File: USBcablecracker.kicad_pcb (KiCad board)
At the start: 2 copper layers, 100 x 71 mm, 52 parts, among them IC1 ATTINY85-S, P1 USB_A_L, P10 USB_A_R, P11 USB_B_R, P12 CONN_01X06, P2 USB_B_L, P3 USB_TYPEC-S, P4 USB_MINI_L, P5 USB_MICRO_L, P6 USB_OTG, P7 USB_MINI_R, P8 USB_MICRO_R, P9 USB_TYPEC-S, Q1 S8050, SW1 Switch_SPDT_x2, U1 PCF8574, U2 LMV358, U3 AD623

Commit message: update pcb
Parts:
- removed D5: BLUE, LEDs:LED_0603
- removed D6: RED, LEDs:LED_0603
- removed IC1: ATTINY85-S, Housings_SOIC:SOIJ-8_5.3x5.3mm_Pitch1.27mm
- removed Q1: S8050, TO_SOT_Packages_SMD:SOT-23_Handsoldering
- removed R20: 470R, Resistors_SMD:R_0603_HandSoldering
- removed R21: 1K, Resistors_SMD:R_0603_HandSoldering
- removed RV1: POT, USBcablecracker:BOURNS-3362P_pot
- added C7: 1uF, Capacitors_SMD:C_0603_HandSoldering, B.Cu at (74.5, 74.4)
- added C8: 22uF, Capacitors_Tantalum_SMD:Tantalum_Case-A_EIA-3216-18_Wave, B.Cu at (74.6, 81.8)
- added C9: 100nF, Capacitors_SMD:C_0603_HandSoldering, B.Cu at (74.4, 78.9)
- added CONN1: ICSP, Connectors:CONN_2.54mm_2x3, F.Cu at (59.1, 62.5)
- added CONN2: USB_B, SmartEye:USB_Micro-B, F.Cu at (52.6, 85.4)
- added D4: ON, LEDs:LED_0603, F.Cu at (53.4, 76.9)
- added R10: 91R, Resistors_SMD:R_0603_HandSoldering, B.Cu at (113.0, 75.7)
- added Y1: 16MHz, Crystals:crystal_FA238-TSX3225, B.Cu at (75.6, 85.8)
- C1: value 0.1uF -> 22P
- C5: value 4.7uF -> 22P; moved to B.Cu
- C6: value 0.1uF -> 100nF; moved to B.Cu
- D1: value S4 -> RX; footprint AirBox:SOD-323 -> LEDs:LED_0603; moved to F.Cu
- D2: value W4 -> TX; footprint AirBox:SOD-323 -> LEDs:LED_0603; moved to F.Cu
- D3: value W4 -> L; footprint AirBox:SOD-323 -> LEDs:LED_0603; moved to F.Cu
- P12: value CONN_01X06 -> CONN_01X09; footprint Pin_Headers:Pin_Header_Straight_1x06 -> Connectors:CONN_2.54mm_1x9
- P6: value USB_OTG -> CONN_01X09; footprint SmartEye:USB_Micro-B -> Connectors:CONN_2.54mm_1x9
- R13: value 10K -> 100K
- R17: value 10K -> 100R
- R2, R3, R5: value 10K -> 1K; moved to F.Cu
- R4: moved to F.Cu
- R6: value 10K -> 1K
- R7: value 1.5K -> 22R; moved to F.Cu
- R8: value 68R -> 22R; moved to F.Cu
- R9: value 68R -> 10K
- U1: value PCF8574 -> ATmega32U4-AU; footprint Housings_SOIC:SOIC-16W_7.5x10.3mm_Pitch1.27mm -> Housings_QFP:TQFP-44_10x10mm_Pitch0.8mm
- moved P6 85.6 mm to (135.5, 64.7), turned to 0 degrees
- moved P12 83.1 mm to (135.3, 106.5)
- moved R1 56.5 mm to (135.0, 73.2), turned to 90 degrees
- moved R5 46.8 mm to (58.8, 76.9), turned to 0 degrees
- moved R4 46.7 mm to (58.8, 74.7), turned to 0 degrees
- moved G*** 39.9 mm to (113.8, 107.7), turned to 180 degrees
- moved C6 38.4 mm to (98.9, 85.7), turned to 90 degrees
- moved C1 34.9 mm to (71.7, 86.0), turned to 270 degrees
- moved D3 26.2 mm to (53.4, 74.7), turned to 0 degrees
- moved D2 25.6 mm to (53.4, 72.5)
- moved D1 24.9 mm to (53.4, 70.4), turned to 180 degrees
- moved R2 23.3 mm to (58.8, 70.4), turned to 0 degrees
- moved R3 21.4 mm to (58.8, 72.5), turned to 0 degrees
- moved R8 20.0 mm to (61.1, 84.2)
- moved R9 19.1 mm to (74.5, 76.6), turned to 0 degrees
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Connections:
- C1 pad 1: +5V -> Net-(C1-Pad1)
- C5 pad 1: +5V -> Net-(C5-Pad1)
- C6 pad 1: +5V -> /AREF
- D1 pad 2: +5V -> +5C
- D2 pad 2: GND -> +5C
- D3 pad 1: Net-(D3-Pad1) -> GND
- D3 pad 2: GND -> Net-(D3-Pad2)
- DS1 pad 11: /DB4 -> /D6
- DS1 pad 12: /DB5 -> /D7
- DS1 pad 13: /DB6 -> /IO11
- DS1 pad 14: /DB7 -> /IO12
- DS1 pad 15: /A -> +5C
- DS1 pad 16: /K -> Net-(DS1-Pad16)
- DS1 pad 2: +5V -> +5C
- DS1 pad 3: /VO -> Net-(DS1-Pad16)
- DS1 pad 4: /RS -> /D4
- DS1 pad 5: /RW -> GND
- DS1 pad 6: /CS -> /D5
- P12 pad 1: /AREF -> +5C
- P12 pad 2: Net-(D5-Pad2) -> GND
- P12 pad 3: /SDA -> /IO13
- P12 pad 4: /SCL -> /IO10
- P12 pad 5: Net-(IC1-Pad3) -> /IO9
- P12 pad 6: Net-(IC1-Pad1) -> /D3
- P6 pad 1: Net-(D1-Pad1) -> +5C
- P6 pad 2: Net-(D3-Pad1) -> GND
- P6 pad 3: Net-(D2-Pad1) -> /RESET
- P6 pad 4: Net-(P6-Pad4) -> /A5
- P6 pad 5: GND -> /A4
- P6 pad 6: GND -> /A3
- R1 pad 1: Net-(R1-Pad1) -> +5C
- R1 pad 2: +5V -> /RESET
- R2 pad 1: Net-(R2-Pad1) -> Net-(D1-Pad1)
- R2 pad 2: +5V -> /RX_LED
- R3 pad 1: Net-(R3-Pad1) -> Net-(D2-Pad1)
- R3 pad 2: +5V -> /TX_LED
- R4 pad 1: +5V -> Net-(D3-Pad2)
- R4 pad 2: /P3 -> /IO13
- R5 pad 1: +5V -> Net-(D4-Pad2)
- R5 pad 2: /SCL -> +5C
- R6 pad 1: +5V -> GND
- R6 pad 2: /SDA -> /HWB
- R7 pad 1: +5V -> /D+
- R7 pad 2: Net-(D3-Pad1) -> Net-(CONN2-Pad3)
- R8 pad 1: /SCL -> /D-
- R8 pad 2: Net-(D3-Pad1) -> Net-(CONN2-Pad2)
- R9 pad 1: Net-(IC1-Pad3) -> GND
- R9 pad 2: Net-(D2-Pad1) -> +5C
- U1 pad 1: Net-(R1-Pad1) -> /D7
- U1 pad 10: /DB5 -> /MOSI
- U1 pad 11: /DB6 -> /MISO
- U1 pad 12: /DB7 -> /IO11
- U1 pad 13: Net-(U1-Pad13) -> /RESET
- U1 pad 14: /SCL -> +5C
- U1 pad 15: /SDA -> GND
- U1 pad 16: +5V -> Net-(C5-Pad1)
- U1 pad 2: Net-(R2-Pad1) -> +5C
- U1 pad 3: Net-(R3-Pad1) -> /D-
- U1 pad 4: /RS -> /D+
- U1 pad 5: /RW -> GND
- U1 pad 6: /CS -> +5C
- U1 pad 7: /P3 -> +5C
- U1 pad 8: GND -> /RX_LED
- U1 pad 9: /DB4 -> /SCK
- U2 pad 8: +5V -> +5C
- U3 pad 6: /TO_ADC -> /IO8
- U3 pad 7: +5V -> +5C
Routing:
- net +5C: track 0.00 -> 264.8 mm, vias 0 -> 1
- net +5V: track 178.3 -> 0.00 mm
- net /RESET: track 0.00 -> 133.2 mm, vias 0 -> 2
- net /IO13: track 0.00 -> 105.8 mm, vias 0 -> 1
- net /SDA: track 96.2 -> 0.00 mm, vias 2 -> 0
- net /SCL: track 93.9 -> 0.00 mm, vias 2 -> 0
- net /D1: track 0.00 -> 67.2 mm
- net /D3: track 0.00 -> 66.5 mm
- net /D2: track 0.00 -> 65.6 mm
- net Net-(D5-Pad2): track 64.1 -> 0.00 mm, vias 1 -> 0
- net /D0: track 0.00 -> 62.1 mm
- net /IO10: track 0.00 -> 61.7 mm, vias 0 -> 1
- net /IO9: track 0.00 -> 60.3 mm, vias 0 -> 1
- net /A5: track 0.00 -> 59.7 mm, vias 0 -> 1
- net /AREF: track 101.3 -> 44.7 mm, vias 2 -> 3
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- removed copper zone on B.Cu, net GND
- removed copper zone on F.Cu, net GND
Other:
- net class power added: clearance 0.2, trace_width 0.4, via_dia 0.6, via_drill 0.4
- board text added: "13"
- board text added: "P"
- board text added: "R"
- board text added: "T"
- board text added: "v0.2"
- board text removed: "SCL"
- board text removed: "SDA"
- board text removed: "v0.1"

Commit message: update pcb
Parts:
- moved G*** 3.38 mm to (114.9, 104.5)
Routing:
- net GND: track 318.9 -> 472.8 mm, vias 1 -> 23
- net /D7: track 31.2 -> 36.4 mm
- net /D0: track 62.1 -> 65.8 mm
- net /IO11: track 34.8 -> 38.0 mm
- net /A5: track 59.7 -> 61.3 mm
- net /TP2: track 136.8 -> 138.2 mm
- net /D2: track 65.6 -> 66.7 mm
- net /D5: track 11.5 -> 10.8 mm
- net /D4: track 11.6 -> 10.9 mm
- net /MOSI: track 44.7 -> 45.3 mm
- net Net-(DS1-Pad16): track 40.1 -> 39.5 mm
- added copper zone on B.Cu, net GND
- added copper zone on F.Cu, net GND
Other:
- net class Default: trace_width 0.4 -> 0.3

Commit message: check
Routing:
- net GND: track 472.8 -> 586.8 mm, vias 23 -> 33
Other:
- board text added: "A0"
- board text added: "A1"
- board text added: "A2"
- board text added: "A3"
- board text added: "A4"
- board text added: "A5"
- board text added: "D0"
- board text added: "D1"
- board text added: "D10"
- board text added: "D13"
- board text added: "D2"
- board text added: "D3"
- board text added: "D9"
- board text added: "G"
- board text added: "RES"
- board text added: "USBcablecracker"
- board text added: "VCC"

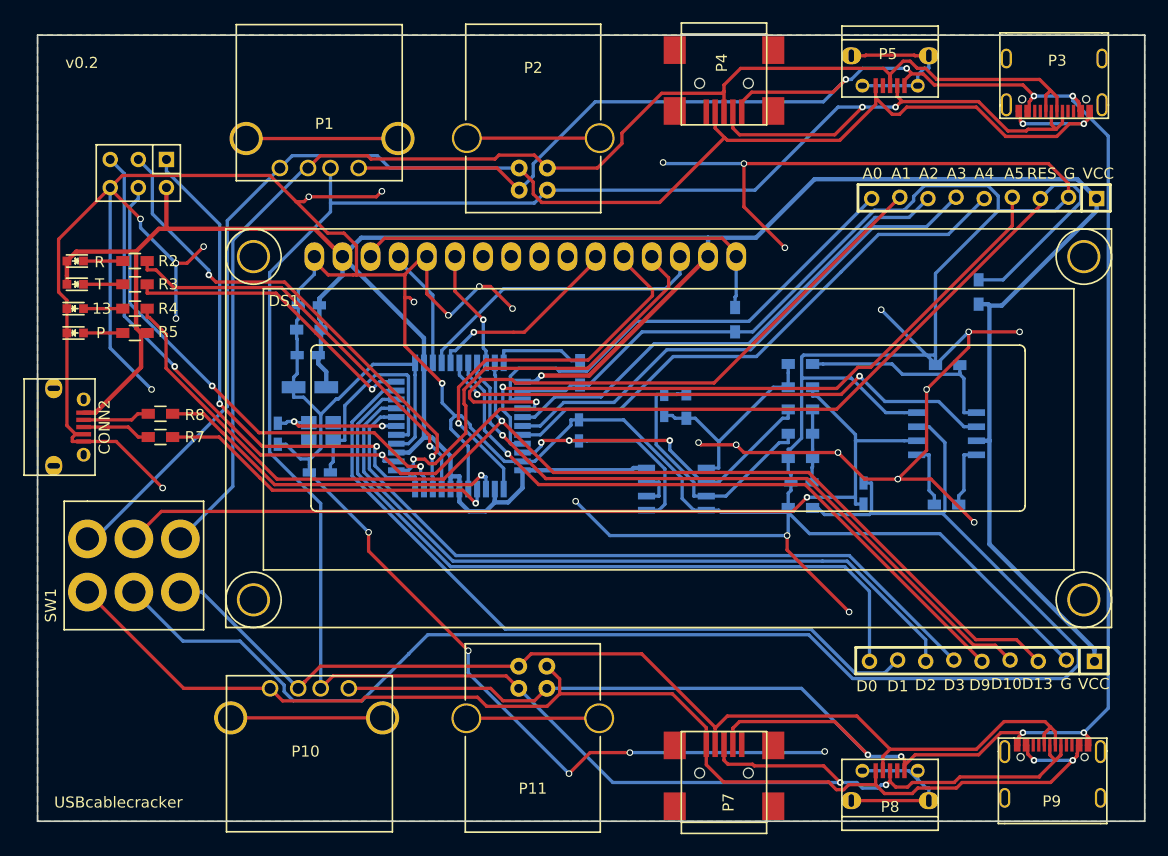
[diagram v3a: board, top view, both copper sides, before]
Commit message: Version 0.4 finished. Solved UCAP inner linear regulator problem. Modified library, footprints, instrumentation amplifier common mode input voltage, modified AREF output load.
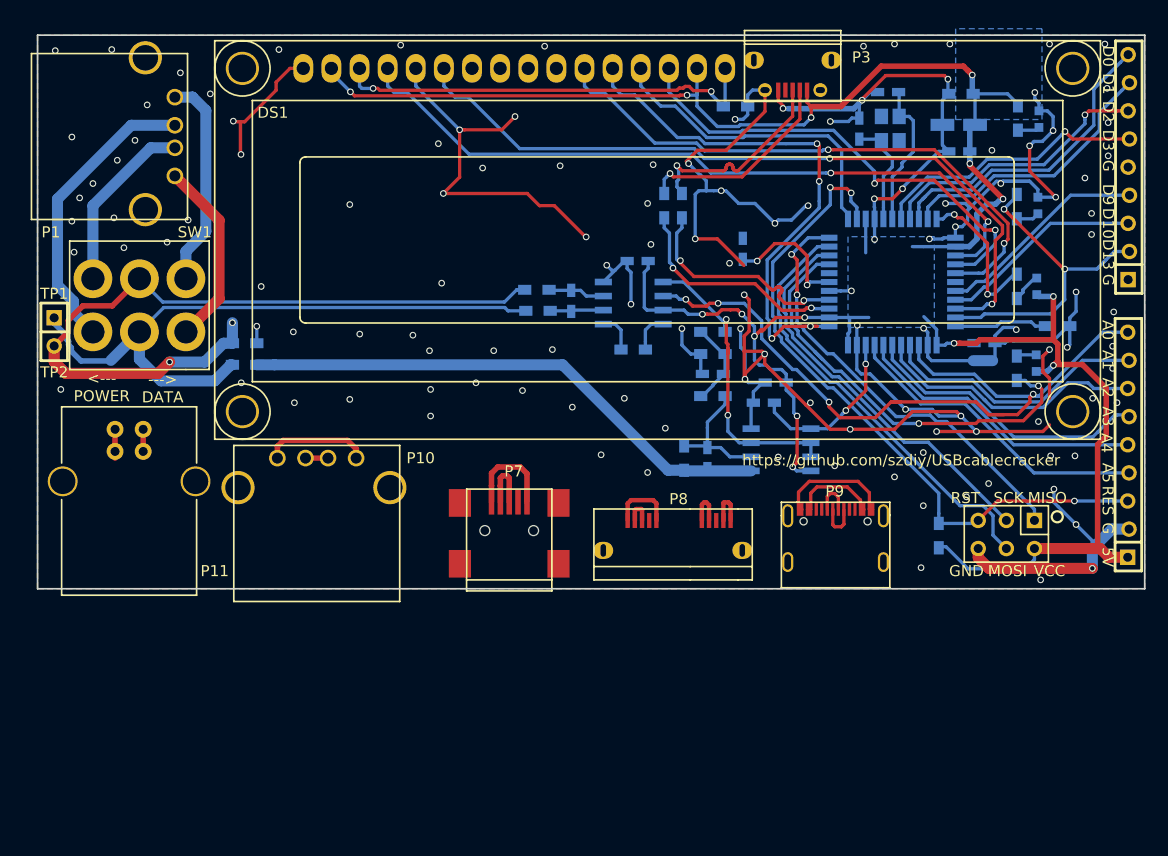
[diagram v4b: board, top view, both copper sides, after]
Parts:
- removed the P3 at (141.5, 53.5)
- removed P4: USB_MINI_L, Connect:USB_Mini-B
- removed P5: USB_MICRO_L, SmartEye:USB_Micro-B
- added C10: 100nF, Capacitors_SMD:C_0603_HandSoldering, B.Cu at (116.7, 81.4)
- added C11: 100nF, Capacitors_SMD:C_0603_HandSoldering, B.Cu at (104.2, 70.4)
- added C12: 100nF, Capacitors_SMD:C_0603_HandSoldering, B.Cu at (135.5, 77.8)
- C1, C5: value 22P -> 15P
- D1, D2, D3, D4, R2, R3, R4, R5, R7, R8: moved to B.Cu
- P1: value USB_A_L -> USB_A; footprint Connect:USB_A -> USBcablecracker:USB_A
- P10: value USB_A_R -> USB_A; footprint Connect:USB_A -> USBcablecracker:USB_A
- P11: value USB_B_R -> USB_B; footprint Connect:USB_B -> USBcablecracker:USB_B
- P12, P6: footprint Connectors:CONN_2.54mm_1x9 -> USBcablecracker:CONN_2.54mm_1x9
- P2: value USB_B_L -> CONN_01X02; footprint Connect:USB_B -> Connectors:CONN_2.54mm_1x2
- P3: renamed from CONN2; value USB_B -> USB_B-Micro; footprint SmartEye:USB_Micro-B -> USBcablecracker:USB_Micro-B
- P7: value USB_MINI_R -> USB_B-Mini; footprint Connect:USB_Mini-B -> USBcablecracker:USB_Mini-B
- P8: value USB_MICRO_R -> USB_B-Micro-3.0; footprint SmartEye:USB_Micro-B -> USBcablecracker:USB_Micro-30
- R15, R16: value 1K -> 10K
- R17: value 100R -> 220
- R18: value 100R -> 150
- R19: value 100R -> 10k
- moved D4 89.2 mm to (140.4, 57.6), turned to 270 degrees
- moved D3 87.4 mm to (140.3, 65.4), turned to 270 degrees
- moved D1 87.3 mm to (140.2, 79.6), turned to 270 degrees
- moved D2 86.8 mm to (140.2, 72.7), turned to 270 degrees
- moved CONN1 84.9 mm to (137.5, 95.1)
- moved R5 82.1 mm to (138.5, 57.5), turned to 90 degrees
- moved R2 80.2 mm to (138.4, 80.1), turned to 270 degrees
- moved R4 80.2 mm to (138.4, 65.5), turned to 90 degrees
- moved R3 79.6 mm to (138.4, 72.7), turned to 90 degrees
- moved P3 73.0 mm to (118.2, 53.4), turned to 180 degrees
- moved C8 63.2 mm to (133.2, 58.1)
- moved C1 63.2 mm to (126.8, 55.1), turned to 180 degrees
- moved R9 62.6 mm to (133.4, 55.3)
- moved C9 61.7 mm to (133.2, 60.5)
- moved Y1 58.2 mm to (127.0, 58.4), turned to 270 degrees
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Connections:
- net Net-(C1-Pad1) renamed /X+
- net Net-(C5-Pad1) renamed /X-
- net Net-(CONN2-Pad2) renamed /DIN-
- net Net-(CONN2-Pad3) renamed /DIN+
- C4 pad 1: /TP1 -> Net-(C4-Pad1)
- C4 pad 2: /TP2 -> Net-(C4-Pad2)
- C7 pad 2: +5C -> Net-(C7-Pad2)
- C8 pad 1: +5C -> +5V
- C9 pad 2: +5C -> +5V
- CONN1 pad 2: +5C -> +5V
- D1 pad 2: +5C -> +5V
- D2 pad 2: +5C -> +5V
- DS1 pad 15: +5C -> +5V
- DS1 pad 2: +5C -> +5V
- P1 pad 1: /TEST1 -> Net-(P1-Pad1)
- P1 pad 2: /TEST2 -> Net-(P1-Pad2)
- P1 pad 3: /TEST3 -> Net-(P1-Pad3)
- P1 pad 4: /TEST4 -> Net-(P1-Pad4)
- P10 pad 1: /TEST5 -> Net-(P10-Pad1)
- P10 pad 2: /TEST6 -> Net-(P10-Pad2)
- P10 pad 3: /TEST2 -> Net-(P10-Pad2)
- P10 pad 4: /TEST1 -> Net-(P10-Pad1)
- P11 pad 1: /TEST5 -> Net-(P11-Pad1)
- P11 pad 2: /TEST6 -> Net-(P11-Pad2)
- P11 pad 3: /TEST2 -> Net-(P11-Pad2)
- P11 pad 4: /TEST1 -> Net-(P11-Pad1)
- P12 pad 1: +5C -> GND
- P12 pad 2: GND -> /IO13
- P12 pad 3: /IO13 -> /IO10
- P12 pad 4: /IO10 -> /IO9
- P12 pad 5: /IO9 -> GND
- P2 pad 1: /TEST1 -> /TP1
- P2 pad 2: /TEST2 -> /TP2
- P3 pad 1: +5C -> +5V
- P3 pad 4: GND -> Net-(P3-Pad4)
- P3 pad 6: (no net) -> GND
- P6 pad 1: +5C -> +5V
- P7 pad 1: /TEST5 -> Net-(P7-Pad1)
- P7 pad 2: /TEST6 -> Net-(P7-Pad2)
- P7 pad 3: /TEST2 -> Net-(P7-Pad2)
- P7 pad 4: /TEST1 -> Net-(P7-Pad4)
- P7 pad 5: Net-(P7-Pad5) -> Net-(P7-Pad1)
- P7 pad 6: (no net) -> Net-(P7-Pad6)
- P8 pad 1: /TEST5 -> Net-(P8-Pad1)
- P8 pad 2: /TEST6 -> Net-(P8-Pad2)
- P8 pad 3: /TEST2 -> Net-(P8-Pad2)
- P8 pad 5: /TEST1 -> Net-(P8-Pad1)
- P9 pad 1: (no net) -> Net-(P9-Pad1)
- P9 pad 2: (no net) -> Net-(P9-Pad2)
- P9 pad 3: (no net) -> Net-(P9-Pad3)
- P9 pad 4: (no net) -> Net-(P9-Pad4)
- R1 pad 1: +5C -> +5V
- R11 pad 1: /AREF -> /REFO
- R15 pad 1: Net-(C3-Pad1) -> Net-(C4-Pad1)
- R15 pad 2: /VOL_HALF -> /TP1
- R16 pad 1: /VOL_HALF -> Net-(C4-Pad2)
- R16 pad 2: GND -> /TP2
- R5 pad 2: +5C -> +5V
- R9 pad 2: +5C -> +5V
- SW1 pad 1: /TEST4 -> Net-(P1-Pad4)
- SW1 pad 3: /TEST3 -> Net-(P1-Pad2)
- SW1 pad 4: /TEST5 -> Net-(P1-Pad1)
- SW1 pad 6: /TEST6 -> Net-(P1-Pad3)
- U1 pad 14: +5C -> +5V
- U1 pad 2: +5C -> +5V
- U1 pad 24: +5C -> +5V
- U1 pad 34: +5C -> +5V
- U1 pad 44: +5C -> +5V
- U1 pad 6: +5C -> Net-(C7-Pad2)
- U2 pad 2: /AREF -> Net-(C3-Pad2)
- U2 pad 3: Net-(C3-Pad2) -> /REFO
- U2 pad 6: Net-(U2-Pad6) -> /REFO
- U2 pad 7: Net-(U2-Pad6) -> /REFO
- U2 pad 8: +5C -> +5V
- U3 pad 2: /TP1 -> Net-(C4-Pad1)
- U3 pad 3: /TP2 -> Net-(C4-Pad2)
- U3 pad 5: /VOL_HALF -> /REFO
- U3 pad 6: /IO8 -> /A0
- U3 pad 7: +5C -> +5V
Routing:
- net GND: track 586.8 -> 308.4 mm, vias 33 -> 50
- net +5C: track 264.7 -> 0.00 mm, vias 1 -> 0
- net /TEST2: track 232.2 -> 4.17 mm, vias 4 -> 0
- net /TEST1: track 238.7 -> 10.9 mm, vias 8 -> 0
- net +5V: track 0.00 -> 213.0 mm, vias 0 -> 15
- net /TEST4: track 136.9 -> 0.00 mm, vias 2 -> 0
- net /TEST3: track 120.7 -> 0.00 mm
- net /TEST5: track 113.6 -> 8.15 mm, vias 2 -> 0
- net /TEST6: track 98.3 -> 3.53 mm
- net /IO13: track 105.8 -> 29.5 mm, vias 1 -> 2
- net /RESET: track 133.2 -> 61.6 mm, vias 2 -> 3
- net /TP2: track 138.2 -> 68.1 mm, vias 0 -> 2
- net /D5: track 10.8 -> 68.2 mm, vias 1 -> 2
- net /D4: track 10.9 -> 66.3 mm, vias 0 -> 2
- net /IO8: track 51.2 -> 0.00 mm, vias 2 -> 0
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- added copper zone on B.Cu, net +5V
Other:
- board size 100 x 71 mm -> 100 x 50 mm
- rule trace_min: 0.2 -> 0.3
- board text added: "---> DATA"
- board text added: "5V"
- board text added: "<--- POWER"
- board text added: "GND"
- board text added: "MISO"
- board text added: "MOSI"
- board text added: "PWR"
- board text added: "RST"
- board text added: "RX"
- board text added: "SCK"
- board text added: "SZDIY COMMUNITY 2009.4.19-2017.4.19"
- board text added: "TP1"
- board text added: "TP2"
- board text added: "TX"
- board text added: "https://github.com/szdiy/USBcablecracker"
- board text removed: "13"
- board text removed: "P"
- board text removed: "R"
- board text removed: "T"
- board text removed: "USBcablecracker"
- board text removed: "v0.2"

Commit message: fangzhou
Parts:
- moved G*** 0.22 mm to (78.9, 66.6)
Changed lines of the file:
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@@
     (links 149)
     (no_connects 0)
-    (area 49.924999 49.924999 150.075001 100.075001)
+    (area 47.6808 47.625 152.53256 101.955)
     (thickness 1.6)
     (drawings 39)
@@
   )
   (module USBcablecracker:donotcare (layer B.Cu)
-    (at 78.8 66.8 180)
+    (at 78.9 66.6 180)
     (fp_text reference G*** (at 0 0 180) (layer B.SilkS) hide
       (effects (font (thickness 0.3)) (justify mirror))

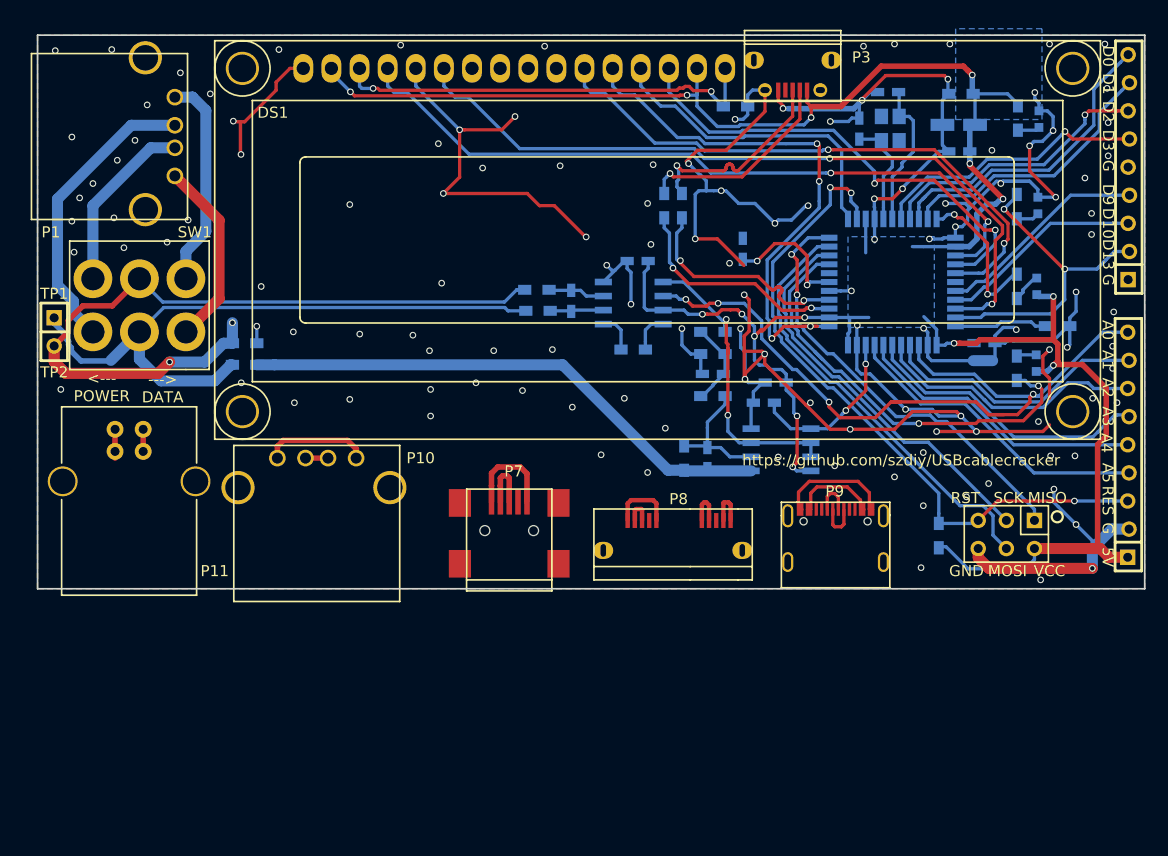
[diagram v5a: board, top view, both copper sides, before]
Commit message: Modified two 9-pin header distance and modified all via with not net to net GND. Add gitinore file.
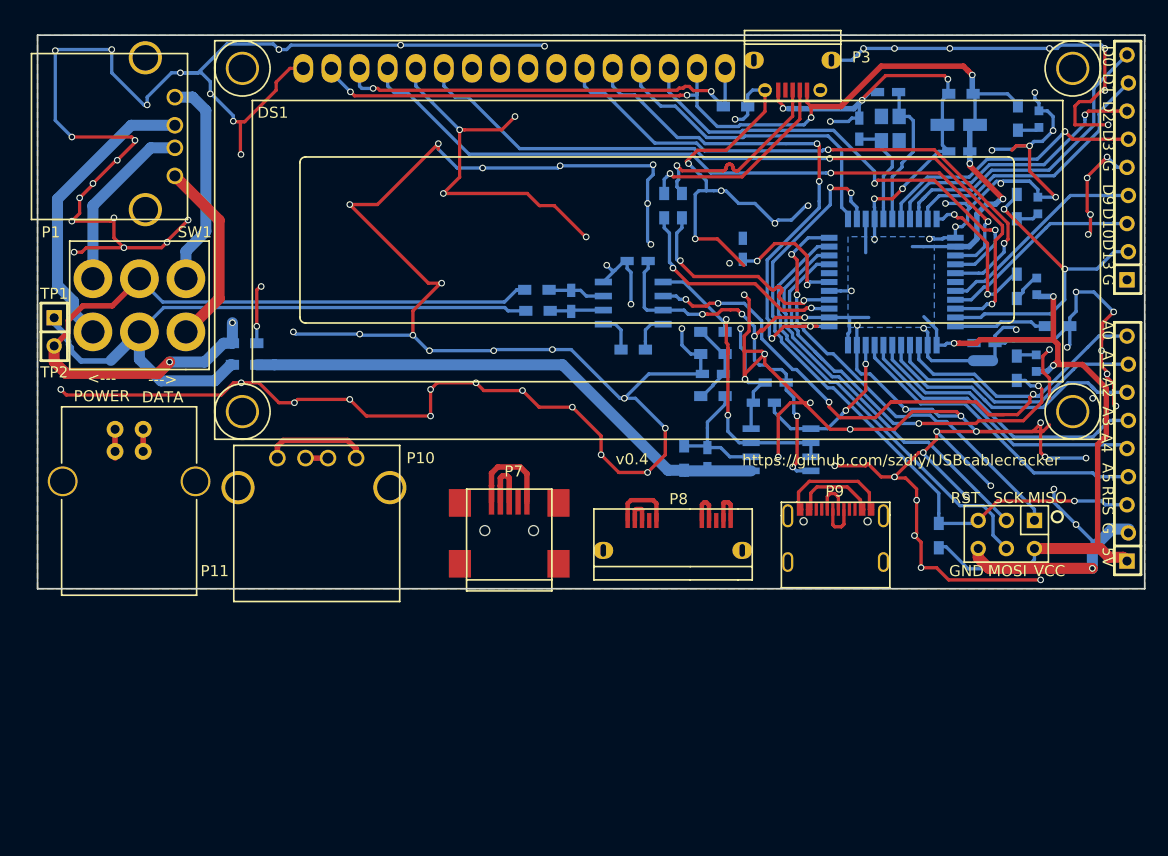
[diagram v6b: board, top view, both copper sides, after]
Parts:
- moved P6 0.35 mm to (148.5, 87.3)
- moved P12 0.10 mm to (148.5, 61.9)
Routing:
- net GND: track 308.4 -> 712.8 mm, vias 50 -> 126
- net (no net): vias 78 -> 3
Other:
- board text added: "v0.4"
